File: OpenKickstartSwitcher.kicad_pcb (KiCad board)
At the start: 2 copper layers, 25.7 x 78.5 mm, 13 parts, among them J1 Conn_01x03, J2 Conn_01x04, J4 Conn_01x03, J98 LOGO, J99 OSHW_LOGO, U1 KS_SOCKET, U2 M27C800, U3 7400

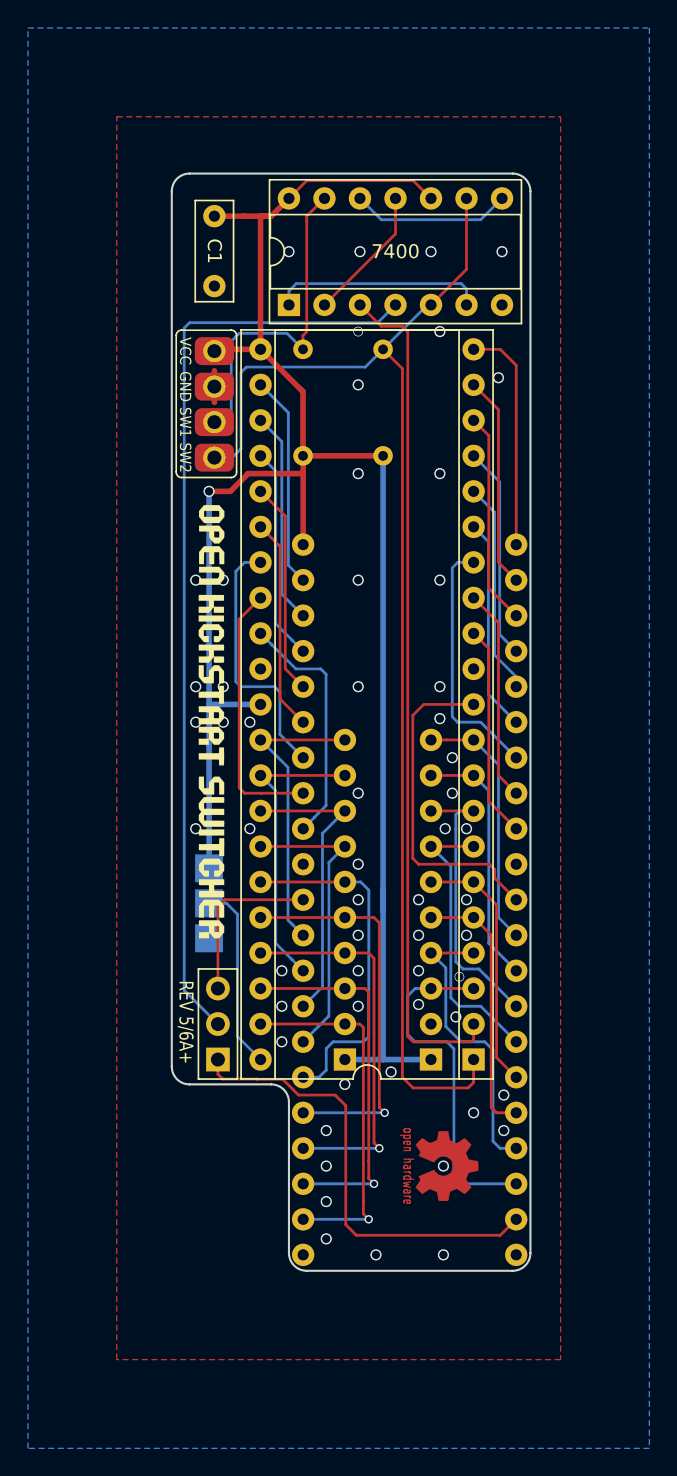
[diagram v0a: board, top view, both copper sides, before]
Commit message: Remove revision jumper and other cosmetic fixes
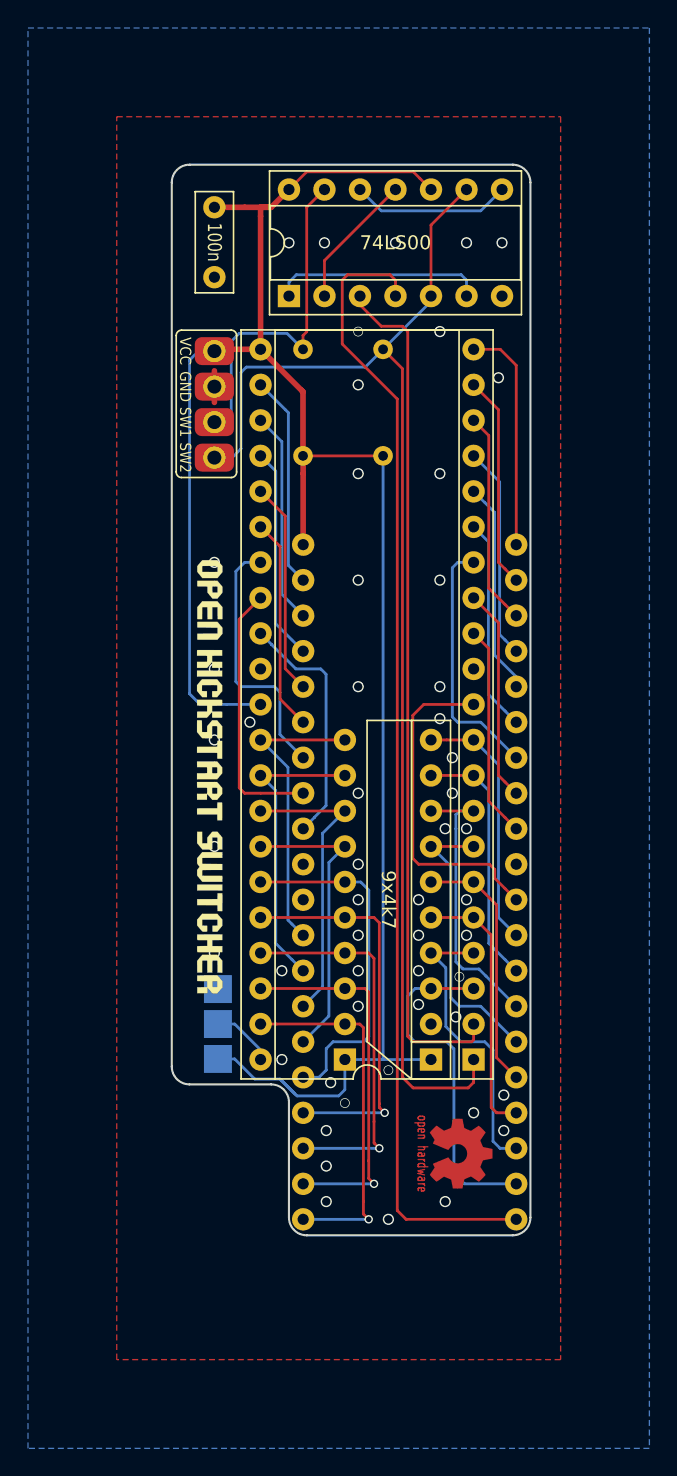
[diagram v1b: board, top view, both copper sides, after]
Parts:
- removed J1: Conn_01x03, OpenKickstartSwitcher:Pin_Header_Straight_1x03-ModSilkS
- RN1: value 4.7k -> 9x4k7; footprint Resistor_THT:R_Array_SIP10 -> OpenKickstartSwitcher:R_Array_SIP10_OnSide; moved to F.Cu
- RN2: value 4.7k -> 9x4k7; footprint Resistor_THT:R_Array_SIP10 -> OpenKickstartSwitcher:R_Array_SIP10_OnSide
- U1: footprint OpenKickstartSwitcher:DIP-42_DualHeaderStrips -> OpenKickstartSwitcher:DIP-40_DualHeaderStrips
- moved J4 8.66 mm to (146.9, 147.4), turned to 90 degrees
- moved J98 3.94 mm to (146.3, 129.8)
- moved U1 2.54 mm to (168.3, 161.4)
- moved J99 1.35 mm to (164.3, 156.7)
- moved C1 0.64 mm to (146.7, 89.0)
- moved U3 0.64 mm to (152.0, 95.4)
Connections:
- U1 pad 1: Net-(U1-Pad1) -> /a17
- U1 pad 10: /a0 -> Net-(U1-Pad10)
- U1 pad 11: Net-(U1-Pad11) -> GND
- U1 pad 12: GND -> Net-(U1-Pad12)
- U1 pad 13: Net-(U1-Pad13) -> /d0
- U1 pad 14: /d0 -> /d8
- U1 pad 15: /d8 -> /d1
- U1 pad 16: /d1 -> /d9
- U1 pad 17: /d9 -> /d2
- U1 pad 18: /d2 -> /d10
- U1 pad 19: /d10 -> /d3
- U1 pad 2: Net-(J1-Pad1) -> /a7
- U1 pad 20: /d3 -> /d11
- U1 pad 21: /d11 -> VCC
- U1 pad 22: VCC -> /d4
- U1 pad 23: /d4 -> /d12
- U1 pad 24: /d12 -> /d5
- U1 pad 25: /d5 -> /d13
- U1 pad 26: /d13 -> /d6
- U1 pad 27: /d6 -> /d14
- U1 pad 28: /d14 -> /d7
- U1 pad 29: /d7 -> /d15
- U1 pad 3: /a7 -> /a6
- U1 pad 30: /d15 -> GND
- U1 pad 31: GND -> (no net)
- U1 pad 32: Net-(J1-Pad3) -> /a16
- U1 pad 33: /a16 -> /a15
- U1 pad 34: /a15 -> /a14
- U1 pad 35: /a14 -> /a13
- U1 pad 36: /a13 -> /a12
- U1 pad 37: /a12 -> /a11
- U1 pad 38: /a11 -> /a10
- U1 pad 39: /a10 -> /a9
- U1 pad 4: /a6 -> /a5
- U1 pad 40: /a9 -> /a8
- U1 pad 5: /a5 -> /a4
- U1 pad 6: /a4 -> /a3
- U1 pad 7: /a3 -> /a2
- U1 pad 8: /a2 -> /a1
- U1 pad 9: /a1 -> /a0
- U2 pad 11: Net-(U1-Pad11) -> Net-(U1-Pad10)
- U2 pad 13: Net-(U1-Pad13) -> Net-(U1-Pad12)
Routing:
- net Net-(J1-Pad1): track 33.7 -> 0.00 mm
- net Net-(U1-Pad11): track 23.9 -> 0.00 mm
- net Net-(U1-Pad10): track 0.00 -> 23.9 mm
- net /a17: track 66.6 -> 82.2 mm
- net Net-(U1-Pad13): track 15.2 -> 0.00 mm
- net Net-(U1-Pad12): track 0.00 -> 15.2 mm
- net Net-(J1-Pad3): track 12.1 -> 0.00 mm
- net Net-(J4-Pad2): track 13.4 -> 4.51 mm
- net VCC: track 140.9 -> 147.3 mm, vias 1 -> 0
- net /sw17: track 24.1 -> 24.7 mm
- net GND: track 2.26 -> 2.32 mm, vias 57 -> 53
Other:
- board size 25.7 x 78.5 mm -> 25.7 x 76.6 mm
- board text added: "74LS00"
- board text added: "github.com/SukkoPera/ OpenKickstartSwitcherCDTV"
- board text removed: "7400"
- board text removed: "REV 5/6A+"
- board text removed: "github.com/SukkoPera/ OpenKickstartSwitcher"
